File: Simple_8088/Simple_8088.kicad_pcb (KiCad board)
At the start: 2 copper layers, 95.1 x 58.2 mm, 21 parts, among them J1 Conn_02x22_Counter_Clockwise, SW1 RESET, U1 8088, U2 74LS257, U3 74LS573, U4 74LS245, U5 74LS04, U6 62256, U7 28C256, X1 OSC

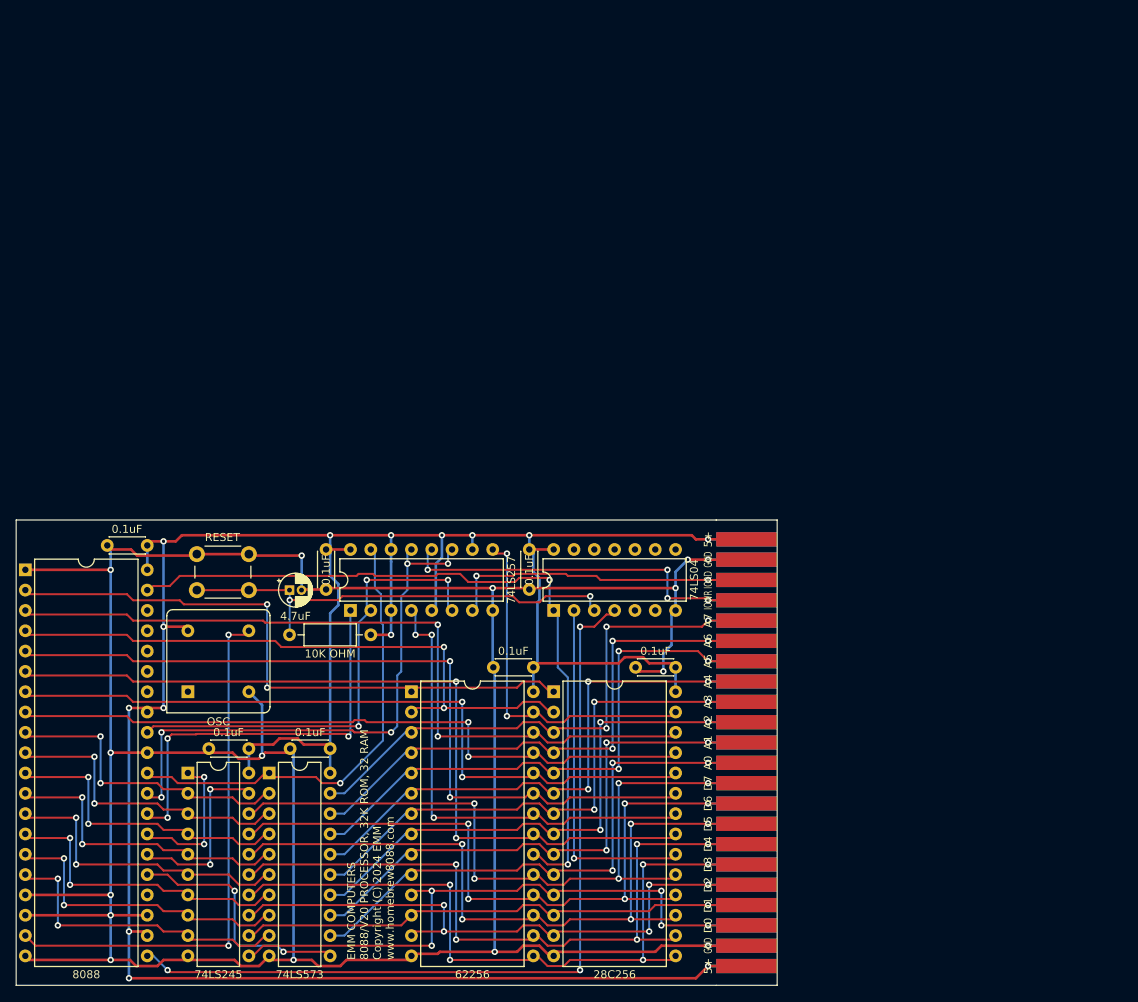
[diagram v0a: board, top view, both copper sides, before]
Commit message: Changing RAM
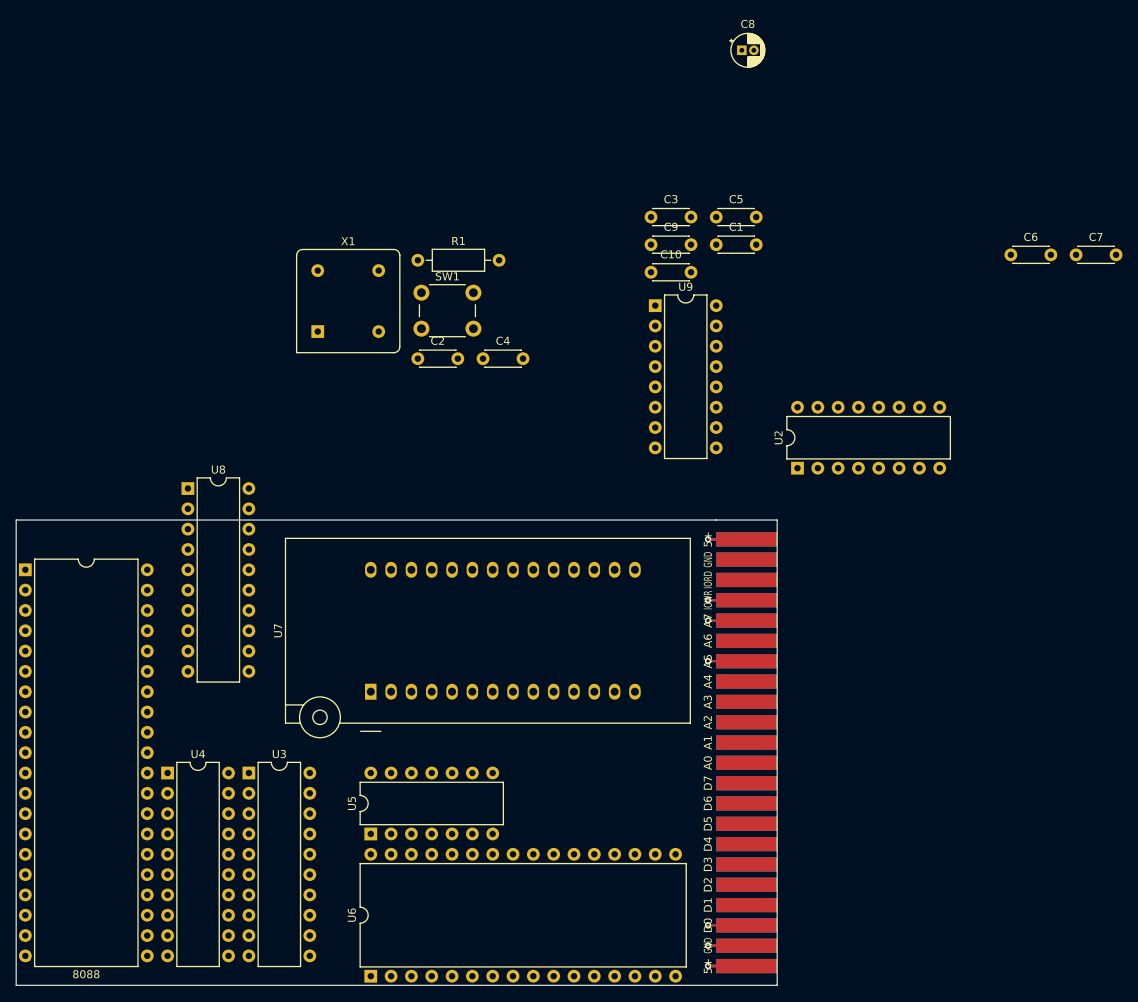
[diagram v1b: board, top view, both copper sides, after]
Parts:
- added C10: 0.1uF, Capacitor_THT:C_Disc_D4.3mm_W1.9mm_P5.00mm, F.Cu at (182.3, 51.7)
- added C9: 0.1uF, Capacitor_THT:C_Disc_D4.3mm_W1.9mm_P5.00mm, F.Cu at (182.3, 48.3)
- added U8: 74LS573, Package_DIP:DIP-20_W7.62mm, F.Cu at (124.5, 78.7)
- added U9: 74LS138, Package_DIP:DIP-16_W7.62mm, F.Cu at (182.9, 55.9)
- U6: value 62256 -> AS6C4008; footprint Package_DIP:DIP-28_W15.24mm -> Package_DIP:DIP-32_W15.24mm
- U7: value 28C256 -> 27C512; footprint Package_DIP:DIP-28_W15.24mm -> Socket:DIP_Socket-28_W11.9_W12.7_W15.24_W17.78_W18.5_3M_228-1277-00-0602J
- moved C8 88.0 mm to (193.7, 24.0)
- moved C1 84.9 mm to (190.5, 48.3)
- moved C6 82.7 mm to (227.3, 49.5)
- moved C3 80.3 mm to (182.3, 44.8)
- moved C7 75.4 mm to (235.5, 49.5)
- moved C4 59.6 mm to (161.3, 62.5)
- moved U2 58.6 mm to (200.7, 76.2)
- moved C5 52.1 mm to (190.5, 44.8), turned to 0 degrees
- moved R1 49.5 mm to (153.2, 50.2)
- moved X1 47.9 mm to (140.7, 59.1)
- moved SW1 43.1 mm to (153.7, 54.3)
- moved U5 36.1 mm to (147.3, 121.9)
- moved U6 35.9 mm to (147.3, 139.7), turned to 90 degrees
- moved C2 31.0 mm to (153.2, 62.5), turned to 0 degrees
- moved U7 22.9 mm to (147.3, 104.1), turned to 90 degrees
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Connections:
- J1 pad 10: /A2 -> Net-(J1-Pad10)
- J1 pad 11: /A1 -> Net-(J1-Pad11)
- J1 pad 12: /A0 -> Net-(J1-Pad12)
- J1 pad 13: /D7 -> Net-(J1-Pad13)
- J1 pad 14: /D6 -> Net-(J1-Pad14)
- J1 pad 15: /D5 -> Net-(J1-Pad15)
- J1 pad 16: /D4 -> Net-(J1-Pad16)
- J1 pad 17: /D3 -> Net-(J1-Pad17)
- J1 pad 18: /D2 -> Net-(J1-Pad18)
- J1 pad 19: /D1 -> Net-(J1-Pad19)
- J1 pad 20: /D0 -> Net-(J1-Pad20)
- J1 pad 3: /IORD -> Net-(J1-Pad3)
- J1 pad 4: /IOWR -> Net-(J1-Pad4)
- J1 pad 5: /A7 -> Net-(J1-Pad5)
- J1 pad 6: /A6 -> Net-(J1-Pad6)
- J1 pad 7: /A5 -> Net-(J1-Pad7)
- J1 pad 8: /A4 -> Net-(J1-Pad8)
- J1 pad 9: /A3 -> Net-(J1-Pad9)
- U1 pad 18: /GND -> /INTR
- U1 pad 35: Net-(U1-Pad35) -> /A19_
- U1 pad 36: Net-(U1-Pad36) -> /A18_
- U1 pad 37: Net-(U1-Pad37) -> /A17_
- U1 pad 38: Net-(U1-Pad38) -> /A16_
- U5 pad 1: /A15 -> /RESET
- U5 pad 2: /A15_ -> /RESET_
- U5 pad 3: /RESET -> Net-(U5-Pad3)
- U5 pad 4: /RESET_ -> Net-(U5-Pad4)
- U6 pad 1: /A14 -> /A18
- U6 pad 10: /A0 -> /A2
- U6 pad 11: /D0 -> /A1
- U6 pad 12: /D1 -> /A0
- U6 pad 13: /D2 -> /D0
- U6 pad 14: /GND -> /D1
- U6 pad 15: /D3 -> /D2
- U6 pad 16: /D4 -> /GND
- U6 pad 17: /D5 -> /D3
- U6 pad 18: /D6 -> /D4
- U6 pad 19: /D7 -> /D5
- U6 pad 2: /A12 -> /A16
- U6 pad 20: /A15 -> /D6
- U6 pad 21: /A10 -> /D7
- U6 pad 22: /MRD -> /512K_CS
- U6 pad 23: /A11 -> /A10
- U6 pad 24: /A9 -> /MRD
- U6 pad 25: /A8 -> /A11
- U6 pad 26: /A13 -> /A9
- U6 pad 27: /MWR -> /A8
- U6 pad 28: /5+ -> /A13
- U6 pad 3: /A7 -> /A14
- U6 pad 4: /A6 -> /A12
- U6 pad 5: /A5 -> /A7
- U6 pad 6: /A4 -> /A6
- U6 pad 7: /A3 -> /A5
- U6 pad 8: /A2 -> /A4
- U6 pad 9: /A1 -> /A3
- U7 pad 1: /A14 -> /A15
- U7 pad 20: /A15_ -> /MRD
- U7 pad 22: /MRD -> /ROM_CS
- U7 pad 27: /MWR -> /A14
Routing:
- net /GND: track 400.3 -> 10.4 mm, vias 15 -> 1
- net /5+: track 352.3 -> 19.3 mm, vias 14 -> 2
- net /RESET_: track 103.1 -> 0.00 mm, vias 3 -> 0
- net /A10: track 102.6 -> 0.72 mm, vias 2 -> 0
- net /A11: track 100.1 -> 0.72 mm, vias 2 -> 0
- net /D7: track 97.3 -> 0.00 mm, vias 5 -> 0
- net /D6: track 96.5 -> 0.00 mm, vias 5 -> 0
- net /A13: track 97.2 -> 0.72 mm, vias 2 -> 0
- net /D5: track 95.8 -> 0.00 mm, vias 5 -> 0
- net /D4: track 95.0 -> 0.00 mm, vias 5 -> 0
- net /D3: track 94.2 -> 0.00 mm, vias 5 -> 0
- net /A15: track 93.4 -> 0.00 mm, vias 2 -> 0
- net /A9: track 92.5 -> 0.72 mm, vias 2 -> 0
- net /A8: track 87.6 -> 0.72 mm, vias 2 -> 0
- net /D2: track 82.1 -> 0.00 mm, vias 5 -> 0
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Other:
- board text removed: "EMM COMPUTERS 8088/V20 PROCESSOR, 32K ROM, 32 RAM Copyright (C) 2024 EMM www.homebrew8088.com"
